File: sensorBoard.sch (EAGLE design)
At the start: 30 parts, among them Q1 BSS84, U1 ADXL345, U2 L3G4200D, U3 MPL115A, X1 22-23-2051

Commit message: Stuff checked, freeze design
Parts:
- added C12: 100n, rcl:C-EUC0402
- added C13: 470n, rcl:C-EUC0402
- added D1: BAT60J, diode:BAT60J
- added R1: 10k, rcl:R-EU_R0402
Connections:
- new net N$8: C12.1, U3.CAP
- new net N$9: C13.2, R1.2
- net GND: now also C12.2, R1.1, U1.SDO, U2.RSVDG@0, U2.SDO
- net N$1: now also C13.1
- net N$5: now also D1.A
- net VBAT: now also D1.C
- net VCC: now also U1.CS, U2.CS
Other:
- moved on the sheet: C8, U3
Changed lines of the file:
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@@
 <part name="C10" library="rcl" deviceset="C-EU" device="C0603"/>
 <part name="C11" library="rcl" deviceset="C-EU" device="C0603"/>
+<part name="C12" library="rcl" deviceset="C-EU" device="C0402" value="100n"/>
+<part name="D1" library="diode" deviceset="BAT60J" device="">
+<attribute name="OC_FARNELL" value="1466524"/>
+</part>
+<part name="GND11" library="supply1" deviceset="GND" device=""/>
+<part name="C13" library="rcl" deviceset="C-EU" device="C0402" value="470n"/>
+<part name="R1" library="rcl" deviceset="R-EU_" device="R0402" value="10k"/>
 </parts>
 <sheets>
@@
 <attribute name="OC_FARNELL" x="96.52" y="27.94" size="1.778" layer="96" display="off"/>
 </instance>
-<instance part="P+4" gate="VCC" x="76.2" y="48.26"/>
+<instance part="P+4" gate="VCC" x="76.2" y="50.8"/>
 <instance part="GND4" gate="1" x="76.2" y="7.62"/>
 <instance part="C3" gate="G$1" x="76.2" y="33.02"/>
@@
 <instance part="P+5" gate="VCC" x="167.64" y="50.8"/>
 <instance part="C7" gate="G$1" x="170.18" y="20.32"/>
-<instance part="U3" gate="G$1" x="157.48" y="88.9">
-<attribute name="OC_FARNELL" x="157.48" y="88.9" size="1.778" layer="96" display="off"/>
+<instance part="U3" gate="G$1" x="157.48" y="68.58">
+<attribute name="OC_FARNELL" x="157.48" y="68.58" size="1.778" layer="96" display="off"/>
 </instance>
-<instance part="P+6" gate="VCC" x="142.24" y="101.6"/>
-<instance part="GND7" gate="1" x="139.7" y="78.74"/>
+<instance part="P+6" gate="VCC" x="142.24" y="81.28"/>
+<instance part="GND7" gate="1" x="139.7" y="58.42"/>
 <instance part="U$3" gate="G$1" x="193.04" y="38.1">
 <attribute name="OC_FARNELL" x="193.04" y="38.1" size="1.778" layer="96" display="off"/>
@@
 <instance part="JP5" gate="G$1" x="259.08" y="20.32" rot="R180"/>
 <instance part="U$9" gate="G$1" x="-7.62" y="99.06" rot="R180"/>
-<instance part="C8" gate="G$1" x="139.7" y="91.44"/>
+<instance part="C8" gate="G$1" x="139.7" y="71.12"/>
 <instance part="C9" gate="G$1" x="238.76" y="83.82"/>
 <instance part="C10" gate="G$1" x="5.08" y="99.06" rot="R90"/>
 <instance part="C11" gate="G$1" x="17.78" y="101.6" rot="R180"/>
+<instance part="C12" gate="G$1" x="137.16" y="66.04"/>
+<instance part="D1" gate="G$1" x="185.42" y="38.1" rot="R90">
+<attribute name="OC_FARNELL" x="185.42" y="38.1" size="1.778" layer="96" rot="R90" display="off"/>
+</instance>
+<instance part="GND11" gate="1" x="127" y="78.74"/>
+<instance part="C13" gate="G$1" x="119.38" y="22.86"/>
+<instance part="R1" gate="G$1" x="119.38" y="12.7" rot="R90"/>
 </instances>
 <busses>
@@
 <pinref part="U2" gate="G$1" pin="RSVDG@1"/>
 <wire x1="76.2" y1="25.4" x2="76.2" y2="27.94" width="0.1524" layer="91"/>
-<wire x1="76.2" y1="27.94" x2="81.28" y2="27.94" width="0.1524" layer="91"/>
+<wire x1="76.2" y1="27.94" x2="78.74" y2="27.94" width="0.1524" layer="91"/>
 <junction x="76.2" y="25.4"/>
 <pinref part="C3" gate="G$1" pin="2"/>
 <junction x="76.2" y="27.94"/>
 <pinref part="C4" gate="G$1" pin="2"/>
-<wire x1="76.2" y1="12.7" x2="114.3" y2="12.7" width="0.1524" layer="91"/>
+<wire x1="78.74" y1="27.94" x2="81.28" y2="27.94" width="0.1524" layer="91"/>
+<wire x1="76.2" y1="12.7" x2="111.76" y2="12.7" width="0.1524" layer="91"/>
 <junction x="76.2" y="12.7"/>
+<pinref part="U2" gate="G$1" pin="SDO"/>
+<wire x1="111.76" y1="12.7" x2="114.3" y2="12.7" width="0.1524" layer="91"/>
+<wire x1="109.22" y1="35.56" x2="111.76" y2="35.56" width="0.1524" layer="91"/>
+<wire x1="111.76" y1="35.56" x2="111.76" y2="12.7" width="0.1524" layer="91"/>
+<junction x="111.76" y="12.7"/>
+<pinref part="U2" gate="G$1" pin="RSVDG@0"/>
+<wire x1="81.28" y1="30.48" x2="78.74" y2="30.48" width="0.1524" layer="91"/>
+<wire x1="78.74" y1="30.48" x2="78.74" y2="27.94" width="0.1524" layer="91"/>
+<junction x="78.74" y="27.94"/>
+<pinref part="R1" gate="G$1" pin="1"/>
+<wire x1="114.3" y1="12.7" x2="114.3" y2="7.62" width="0.1524" layer="91"/>
+<wire x1="114.3" y1="7.62" x2="119.38" y2="7.62" width="0.1524" layer="91"/>
+<junction x="114.3" y="12.7"/>
 </segment>
 <segment>
@@
 </segment>
 <segment>
+<pinref part="U1" gate="G$1" pin="SDO"/>
+<wire x1="124.46" y1="91.44" x2="127" y2="91.44" width="0.1524" layer="91"/>
+<wire x1="127" y1="91.44" x2="127" y2="81.28" width="0.1524" layer="91"/>
+<pinref part="GND11" gate="1" pin="GND"/>
+</segment>
+<segment>
 <pinref part="U3" gate="G$1" pin="GND"/>
-<wire x1="144.78" y1="86.36" x2="139.7" y2="86.36" width="0.1524" layer="91"/>
-<wire x1="139.7" y1="86.36" x2="139.7" y2="81.28" width="0.1524" layer="91"/>
+<wire x1="144.78" y1="66.04" x2="139.7" y2="66.04" width="0.1524" layer="91"/>
+<wire x1="139.7" y1="66.04" x2="139.7" y2="60.96" width="0.1524" layer="91"/>
 <pinref part="GND7" gate="1" pin="GND"/>
 <pinref part="C8" gate="G$1" pin="2"/>
-<junction x="139.7" y="86.36"/>
+<junction x="139.7" y="66.04"/>
+<pinref part="C12" gate="G$1" pin="2"/>
+<wire x1="137.16" y1="60.96" x2="139.7" y2="60.96" width="0.1524" layer="91"/>
+<junction x="139.7" y="60.96"/>
 </segment>
 <segment>
@@
 <wire x1="193.04" y1="45.72" x2="193.04" y2="48.26" width="0.1524" layer="91"/>
 <label x="193.04" y="48.26" size="1.778" layer="95"/>
+<pinref part="D1" gate="G$1" pin="C"/>
+<wire x1="185.42" y1="40.64" x2="185.42" y2="45.72" width="0.1524" layer="91"/>
+<wire x1="185.42" y1="45.72" x2="193.04" y2="45.72" width="0.1524" layer="91"/>
+<junction x="193.04" y="45.72"/>
 </segment>
 </net>
@@
 <segment>
 <pinref part="U3" gate="G$1" pin="SDA/DIN"/>
-<wire x1="170.18" y1="88.9" x2="175.26" y2="88.9" width="0.1524" layer="91"/>
-<label x="175.26" y="88.9" size="1.778" layer="95"/>
+<wire x1="170.18" y1="68.58" x2="175.26" y2="68.58" width="0.1524" layer="91"/>
+<label x="175.26" y="68.58" size="1.778" layer="95"/>
 </segment>
 <segment>
@@
 <segment>
 <pinref part="U3" gate="G$1" pin="SCLK"/>
-<wire x1="170.18" y1="91.44" x2="175.26" y2="91.44" width="0.1524" layer="91"/>
-<label x="175.26" y="91.44" size="1.778" layer="95"/>
+<wire x1="170.18" y1="71.12" x2="175.26" y2="71.12" width="0.1524" layer="91"/>
+<label x="175.26" y="71.12" size="1.778" layer="95"/>
 </segment>
 <segment>
@@
 <wire x1="96.52" y1="88.9" x2="96.52" y2="93.98" width="0.1524" layer="91"/>
 <junction x="96.52" y="93.98"/>
+<junction x="96.52" y="101.6"/>
+<pinref part="U1" gate="G$1" pin="CS"/>
+<wire x1="96.52" y1="101.6" x2="124.46" y2="101.6" width="0.1524" layer="91"/>
+<wire x1="124.46" y1="101.6" x2="124.46" y2="96.52" width="0.1524" layer="91"/>
 </segment>
 <segment>
@@
 <pinref part="U2" gate="G$1" pin="RSVDV@0"/>
 <wire x1="76.2" y1="40.64" x2="76.2" y2="45.72" width="0.1524" layer="91"/>
+<wire x1="76.2" y1="45.72" x2="76.2" y2="48.26" width="0.1524" layer="91"/>
 <wire x1="81.28" y1="35.56" x2="76.2" y2="35.56" width="0.1524" layer="91"/>
 <wire x1="76.2" y1="35.56" x2="76.2" y2="38.1" width="0.1524" layer="91"/>
@@
 <pinref part="C3" gate="G$1" pin="1"/>
 <junction x="76.2" y="35.56"/>
+<wire x1="76.2" y1="45.72" x2="116.84" y2="45.72" width="0.1524" layer="91"/>
+<wire x1="116.84" y1="45.72" x2="116.84" y2="33.02" width="0.1524" layer="91"/>
+<junction x="76.2" y="45.72"/>
+<pinref part="U2" gate="G$1" pin="CS"/>
+<wire x1="116.84" y1="33.02" x2="109.22" y2="33.02" width="0.1524" layer="91"/>
 </segment>
 <segment>
@@
 <pinref part="U3" gate="G$1" pin="SHDN"/>
 <pinref part="P+6" gate="VCC" pin="VCC"/>
-<wire x1="144.78" y1="83.82" x2="142.24" y2="83.82" width="0.1524" layer="91"/>
-<wire x1="142.24" y1="83.82" x2="142.24" y2="91.44" width="0.1524" layer="91"/>
+<wire x1="144.78" y1="63.5" x2="142.24" y2="63.5" width="0.1524" layer="91"/>
+<wire x1="142.24" y1="63.5" x2="142.24" y2="71.12" width="0.1524" layer="91"/>
 <pinref part="U3" gate="G$1" pin="VDD"/>
-<wire x1="142.24" y1="91.44" x2="142.24" y2="93.98" width="0.1524" layer="91"/>
-<wire x1="142.24" y1="93.98" x2="142.24" y2="99.06" width="0.1524" layer="91"/>
-<wire x1="144.78" y1="91.44" x2="142.24" y2="91.44" width="0.1524" layer="91"/>
-<junction x="142.24" y="91.44"/>
+<wire x1="142.24" y1="71.12" x2="142.24" y2="73.66" width="0.1524" layer="91"/>
+<wire x1="142.24" y1="73.66" x2="142.24" y2="78.74" width="0.1524" layer="91"/>
+<wire x1="144.78" y1="71.12" x2="142.24" y2="71.12" width="0.1524" layer="91"/>
+<junction x="142.24" y="71.12"/>
 <pinref part="C8" gate="G$1" pin="1"/>
-<wire x1="139.7" y1="93.98" x2="142.24" y2="93.98" width="0.1524" layer="91"/>
-<junction x="142.24" y="93.98"/>
+<wire x1="139.7" y1="73.66" x2="142.24" y2="73.66" width="0.1524" layer="91"/>
+<junction x="142.24" y="73.66"/>
 </segment>
 <segment>
@@
 <pinref part="U2" gate="G$1" pin="PLL"/>
 <wire x1="114.3" y1="20.32" x2="109.22" y2="20.32" width="0.1524" layer="91"/>
+<pinref part="C13" gate="G$1" pin="1"/>
+<wire x1="114.3" y1="20.32" x2="114.3" y2="25.4" width="0.1524" layer="91"/>
+<wire x1="114.3" y1="25.4" x2="119.38" y2="25.4" width="0.1524" layer="91"/>
+<junction x="114.3" y="20.32"/>
 </segment>
 </net>
@@
 <pinref part="Q1" gate="G$1" pin="S"/>
 <wire x1="193.04" y1="27.94" x2="193.04" y2="30.48" width="0.1524" layer="91"/>
+<pinref part="D1" gate="G$1" pin="A"/>
+<wire x1="185.42" y1="35.56" x2="185.42" y2="30.48" width="0.1524" layer="91"/>
+<wire x1="185.42" y1="30.48" x2="193.04" y2="30.48" width="0.1524" layer="91"/>
+<junction x="193.04" y="30.48"/>
 </segment>
 </net>
@@
 </segment>
 </net>
+<net name="N$8" class="0">
+<segment>
+<pinref part="C12" gate="G$1" pin="1"/>
+<pinref part="U3" gate="G$1" pin="CAP"/>
+<wire x1="137.16" y1="68.58" x2="144.78" y2="68.58" width="0.1524" layer="91"/>
+</segment>
+</net>
+<net name="N$9" class="0">
+<segment>
+<pinref part="C13" gate="G$1" pin="2"/>
+<pinref part="R1" gate="G$1" pin="2"/>
+</segment>
+</net>

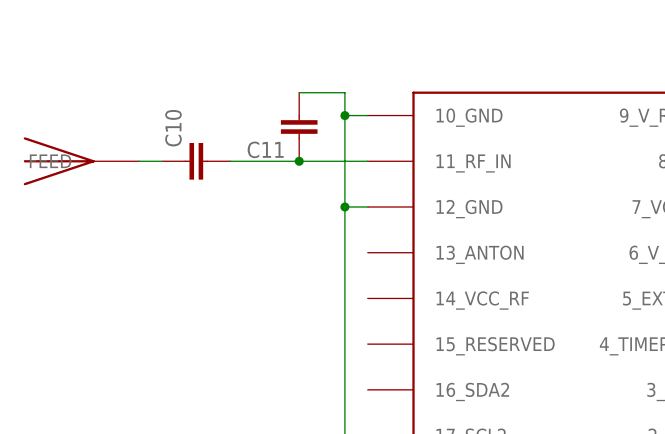
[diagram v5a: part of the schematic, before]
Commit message: Done silk for sensorboard.
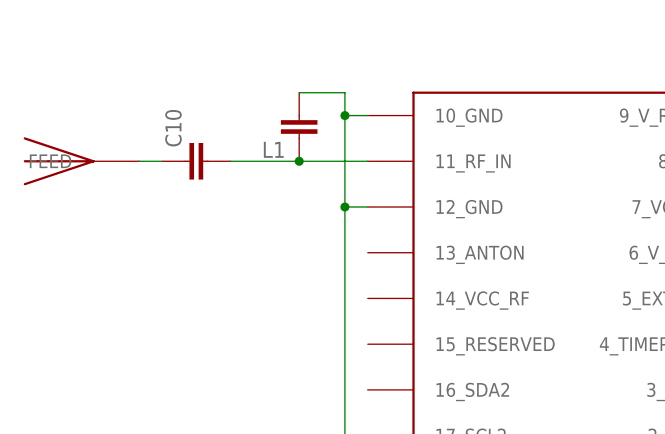
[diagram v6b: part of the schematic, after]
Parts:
- renumbered C11 to L1
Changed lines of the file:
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@@
 <?xml version="1.0" encoding="utf-8"?>
 <!DOCTYPE eagle SYSTEM "eagle.dtd">
-<eagle version="7.2.0">
+<eagle version="7.3.0">
 <drawing>
 <settings>
@@
 <part name="C9" library="rcl" deviceset="C-EU" device="C0402" value="100n"/>
 <part name="C10" library="rcl" deviceset="C-EU" device="C0603"/>
-<part name="C11" library="rcl" deviceset="C-EU" device="C0603"/>
+<part name="L1" library="rcl" deviceset="C-EU" device="C0603"/>
 <part name="C12" library="rcl" deviceset="C-EU" device="C0402" value="100n"/>
 <part name="D1" library="diode" deviceset="BAT60J" device="">
@@
 <instance part="C9" gate="G$1" x="238.76" y="83.82"/>
 <instance part="C10" gate="G$1" x="5.08" y="99.06" rot="R90"/>
-<instance part="C11" gate="G$1" x="17.78" y="101.6" rot="R180"/>
+<instance part="L1" gate="G$1" x="17.78" y="101.6" rot="R180"/>
 <instance part="C12" gate="G$1" x="137.16" y="66.04"/>
 <instance part="D1" gate="G$1" x="185.42" y="38.1" rot="R90">
@@
 <wire x1="22.86" y1="104.14" x2="25.4" y2="104.14" width="0.1524" layer="91"/>
 <junction x="22.86" y="93.98"/>
-<pinref part="C11" gate="G$1" pin="2"/>
+<pinref part="L1" gate="G$1" pin="2"/>
 <wire x1="22.86" y1="104.14" x2="22.86" y2="106.68" width="0.1524" layer="91"/>
 <wire x1="22.86" y1="106.68" x2="17.78" y2="106.68" width="0.1524" layer="91"/>
@@
 <segment>
 <pinref part="C10" gate="G$1" pin="2"/>
-<pinref part="C11" gate="G$1" pin="1"/>
+<pinref part="L1" gate="G$1" pin="1"/>
 <wire x1="10.16" y1="99.06" x2="17.78" y2="99.06" width="0.1524" layer="91"/>
 <pinref part="U$1" gate="G$1" pin="11_RF_IN"/>

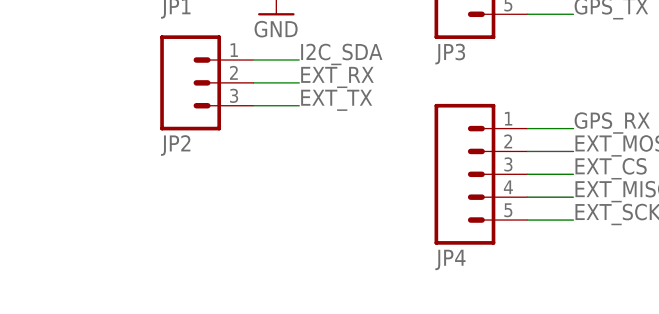
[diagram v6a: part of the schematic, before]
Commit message: Added EARS Logo
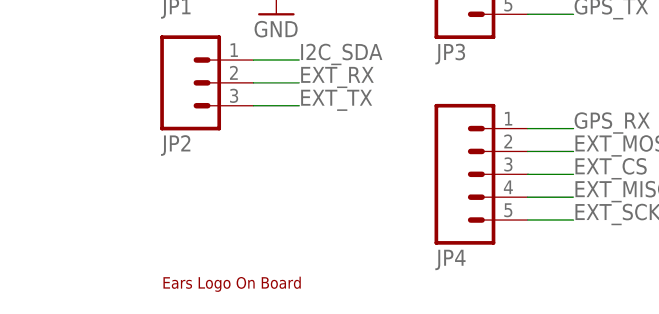
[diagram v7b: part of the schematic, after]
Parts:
- added U$10: EARS-LOGO, earsLogo:EARS-LOGO
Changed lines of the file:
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@@
 <?xml version="1.0" encoding="utf-8"?>
 <!DOCTYPE eagle SYSTEM "eagle.dtd">
-<eagle version="7.3.0">
+<eagle version="7.2.0">
 <drawing>
 <settings>
@@
 <part name="C13" library="rcl" deviceset="C-EU" device="C0402" value="470n"/>
 <part name="R1" library="rcl" deviceset="R-EU_" device="R0402" value="10k"/>
+<part name="U$10" library="earsLogo" deviceset="EARS-LOGO" device=""/>
 </parts>
 <sheets>
@@
 <instance part="C13" gate="G$1" x="119.38" y="22.86"/>
 <instance part="R1" gate="G$1" x="119.38" y="12.7" rot="R90"/>
+<instance part="U$10" gate="G$1" x="2.54" y="0"/>
 </instances>
 <busses>
